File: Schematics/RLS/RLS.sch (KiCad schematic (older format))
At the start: 21 parts, among them J6 ADS1115, U1 ARDUINO_MEGA_SHIELD

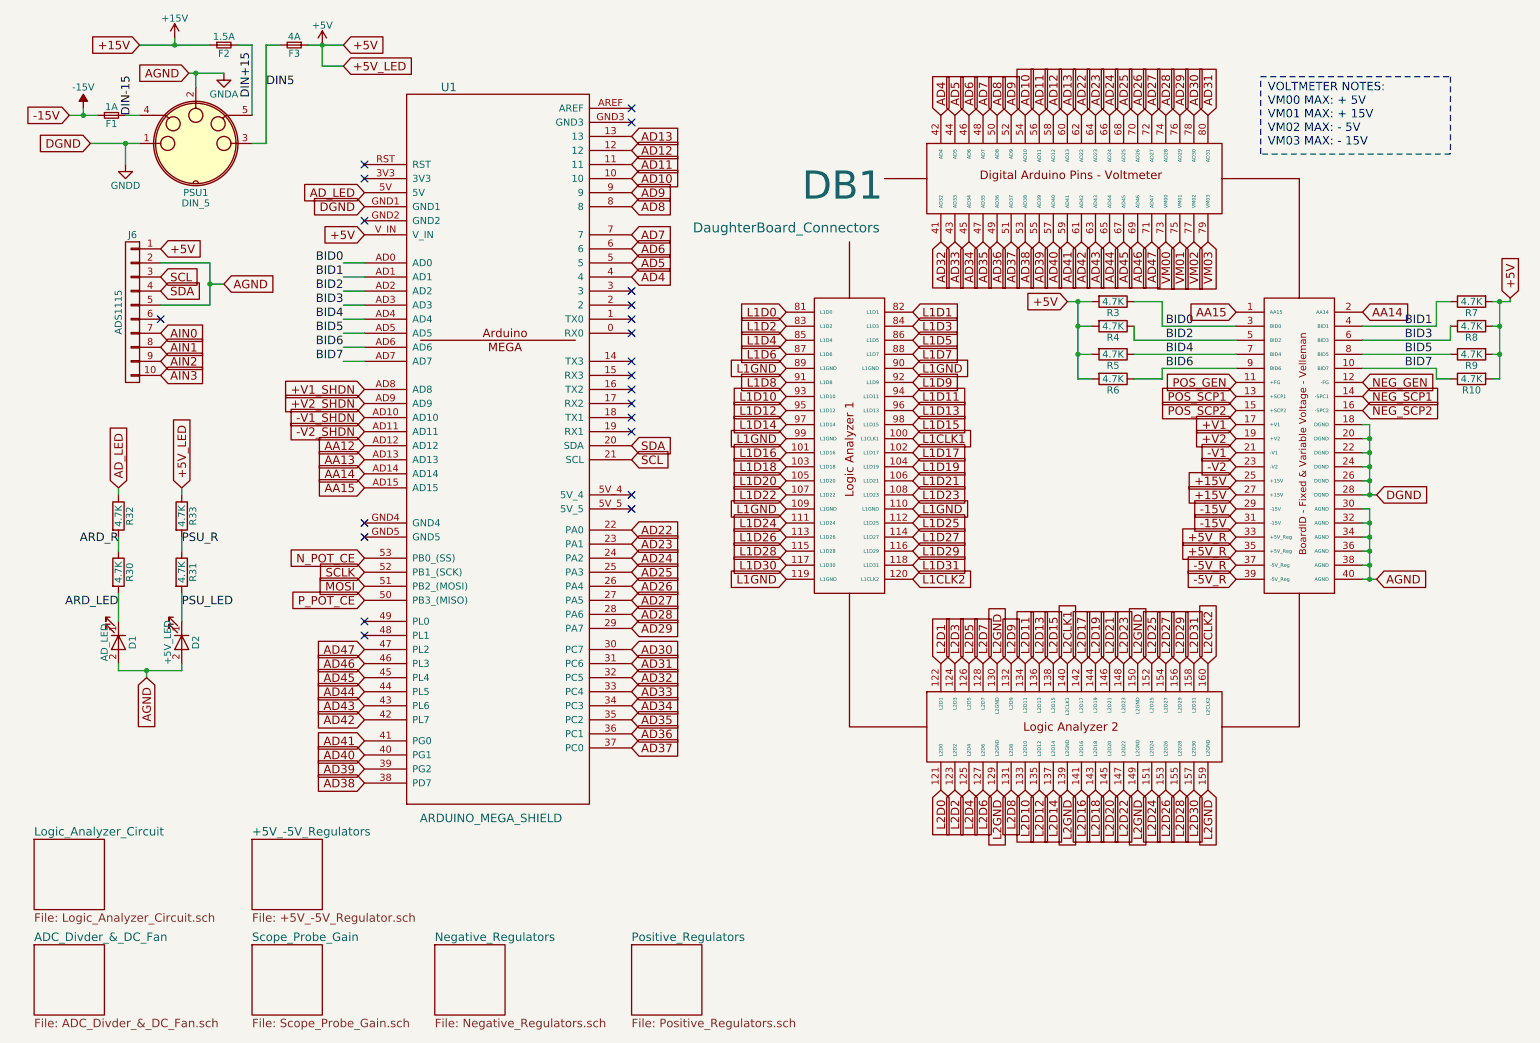
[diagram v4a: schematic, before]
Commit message: Added Things and Fixed Schematic
Added pots to schematic and pcb for adc balancing.
Fixed the component annotation and netlist in the pcb.
Shrunk the pcb down a bit.
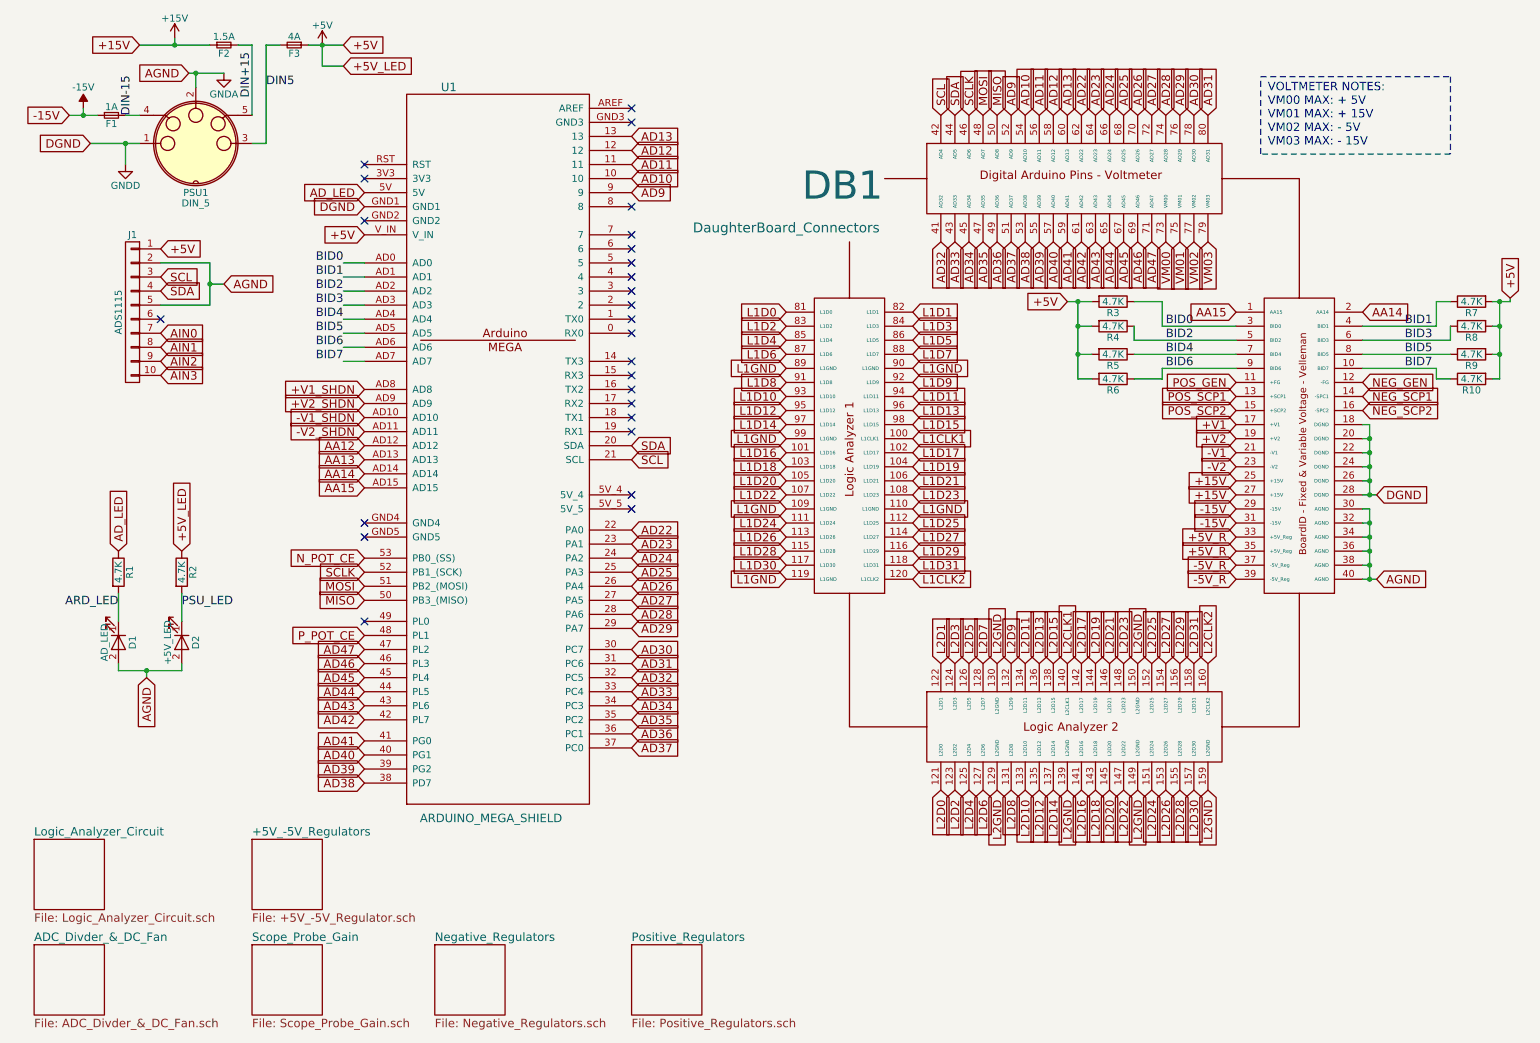
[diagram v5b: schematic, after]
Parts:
- removed R32, R33: 4.7K, Resistors_SMD:R_0805_HandSoldering, symbol R
- renumbered J6 to J1, R30 to R1, R31 to R2
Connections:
- net ARD_R is gone; now on net AD_LED: R1.1
- net PSU_R is gone; now on net +5V: R2.1
- net MOSI: now also DB1.48 (AD7)
- net P_POT_CE: now also U1.48 (PL1); no longer U1.50 (PB3_(MISO))
- net SCL: now also DB1.42 (AD4)
- net SCLK: now also DB1.46 (AD6)
- net SDA: now also DB1.44 (AD5)
- net AD4: no longer names the net of U1.4
- net AD4: no longer DB1.42 (AD4)
- net AD5: no longer names the net of U1.5
- net AD5: no longer DB1.44 (AD5)
- net AD6: no longer names the net of U1.6
- net AD6: no longer DB1.46 (AD6)
- net AD7: no longer names the net of U1.7
- net AD7: no longer DB1.48 (AD7)
- net AD8: no longer names the net of U1.8
- net AD8: no longer DB1.50 (AD8)
- new net MISO: DB1.50 (AD8), U1.50 (PB3_(MISO))
- no-connect marks 22 -> 26
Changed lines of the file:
@@
 $EndDescr
 Text GLabel 7050 1250 1    60   Input ~ 0
-AD4
+SCL
 Text GLabel 7150 1250 1    60   Input ~ 0
-AD5
+SDA
 Text GLabel 7250 1250 1    60   Input ~ 0
-AD6
+SCLK
 Text GLabel 7350 1250 1    60   Input ~ 0
-AD7
+MOSI
 Text GLabel 7450 1250 1    60   Input ~ 0
-AD8
+MISO
 Text GLabel 7550 1250 1    60   Input ~ 0
 AD9
@@
 Text GLabel 7050 6050 3    60   Input ~ 0
 L2D0
-Text GLabel 4850 2400 2    60   Input ~ 0
-AD4
-Text GLabel 4850 2300 2    60   Input ~ 0
-AD5
-Text GLabel 4850 2200 2    60   Input ~ 0
-AD6
-Text GLabel 4850 2100 2    60   Input ~ 0
-AD7
-Text GLabel 4850 1900 2    60   Input ~ 0
-AD8
 Text GLabel 4850 1800 2    60   Input ~ 0
 AD9
@@
 $EndComp
 $Comp
-L CONN_01X10 J6
+L CONN_01X10 J1
 U 1 1 594B108D
 P 1300 2650
-F 0 "J6" H 1300 3200 50  0000 C CNN
+F 0 "J1" H 1300 3200 50  0000 C CNN
 F 1 "ADS1115" V 1400 2650 50  0000 C CNN
 F 2 "Pin_Headers:Pin_Header_Straight_1x10_Pitch2.54mm" H 1300 2650 50  0001 C CNN
@@
 Text GLabel 2950 4400 0    60   Input ~ 0
 N_POT_CE
-Text GLabel 2950 4700 0    60   Input ~ 0
+Text GLabel 2950 4950 0    60   Input ~ 0
 P_POT_CE
 Text GLabel 2950 4500 0    60   Input ~ 0
@@
 NoConn ~ 2950 4250
 NoConn ~ 2950 4850
-NoConn ~ 2950 4950
 NoConn ~ 2950 2000
 NoConn ~ 2950 1700
@@
 $EndComp
 $Comp
-L R R30
+L R R1
 U 1 1 595DC99A
 P 1200 4500
-F 0 "R30" V 1280 4500 50  0000 C CNN
+F 0 "R1" V 1280 4500 50  0000 C CNN
 F 1 "4.7K" V 1200 4500 50  0000 C CNN
 F 2 "Resistors_SMD:R_0805_HandSoldering" V 1130 4500 50  0001 C CNN
@@
 $EndComp
 $Comp
-L R R31
+L R R2
 U 1 1 595DCB07
 P 1650 4500
-F 0 "R31" V 1730 4500 50  0000 C CNN
+F 0 "R2" V 1730 4500 50  0000 C CNN
 F 1 "4.7K" V 1650 4500 50  0000 C CNN
 F 2 "Resistors_SMD:R_0805_HandSoldering" V 1580 4500 50  0001 C CNN
@@
 Text GLabel 2950 1800 0    60   Input ~ 0
 AD_LED
-Text GLabel 1200 3900 1    60   Input ~ 0
+Text GLabel 1200 4350 1    60   Input ~ 0
 AD_LED
-Text GLabel 1650 3900 1    60   Input ~ 0
+Text GLabel 1650 4350 1    60   Input ~ 0
 +5V_LED
 Text GLabel 1400 5250 3    60   Input ~ 0
@@
 	2150 750  2050 750
 Wire Wire Line
-	850  1250 950  1250
-Wire Wire Line
-	950  1250 1050 1250
-Wire Wire Line
-	1350 750  1600 750
-Wire Wire Line
-	1600 750  1850 750
+	850  1250 1050 1250
+Wire Wire Line
+	1350 750  1850 750
 Wire Wire Line
 	1350 1250 1250 1250
@@
 	1500 2300 1850 2300
 Wire Wire Line
-	1850 2300 1850 2450
-Wire Wire Line
-	1850 2450 1850 2600
+	1850 2300 1850 2600
 Wire Wire Line
 	1850 2600 1500 2600
@@
 Connection ~ 1850 2450
 Wire Wire Line
-	10975 2575 11025 2575
-Wire Wire Line
-	11025 2575 11100 2575
-Wire Wire Line
-	11025 2575 11025 2750
-Wire Wire Line
-	11025 2750 11025 2950
-Wire Wire Line
-	11025 2950 11025 3125
+	10975 2575 11100 2575
+Wire Wire Line
+	11025 2575 11025 3125
 Wire Wire Line
 	11025 3125 10975 3125
@@
 	9325 1525 9325 975
 Wire Wire Line
-	1700 950  1750 950
-Wire Wire Line
-	1750 950  1950 950
+	1700 950  1950 950
 Wire Wire Line
 	1750 950  1750 1050
 Wire Wire Line
-	1000 1450 1250 1450
-Wire Wire Line
-	1250 1450 1350 1450
+	1000 1450 1350 1450
 Wire Wire Line
 	1250 1450 1250 1600
@@
 Connection ~ 1750 950
 Wire Wire Line
-	10100 4050 10100 4150
-Wire Wire Line
-	10100 4150 10100 4250
-Wire Wire Line
-	10100 4250 10100 4350
-Wire Wire Line
-	10100 4350 10100 4450
-Wire Wire Line
-	10100 4450 10100 4550
-Wire Wire Line
-	10050 4550 10100 4550
-Wire Wire Line
-	10100 4550 10150 4550
+	10100 4050 10100 4550
+Wire Wire Line
+	10050 4550 10150 4550
 Wire Wire Line
 	10050 4450 10100 4450
@@
 	10050 3450 10100 3450
 Wire Wire Line
-	10100 3450 10100 3550
-Wire Wire Line
-	10100 3550 10100 3650
-Wire Wire Line
-	10100 3650 10100 3750
-Wire Wire Line
-	10100 3750 10100 3850
-Wire Wire Line
-	10100 3850 10100 3950
-Wire Wire Line
-	10050 3950 10100 3950
-Wire Wire Line
-	10100 3950 10150 3950
+	10100 3450 10100 3950
+Wire Wire Line
+	10050 3950 10150 3950
 Wire Wire Line
 	10050 3850 10100 3850
@@
 	2250 750  2250 1450
 Wire Wire Line
-	2550 750  2650 750
-Wire Wire Line
-	2650 750  2800 750
+	2550 750  2800 750
 Connection ~ 2650 750
 Wire Wire Line
 	1650 5200 1650 5150
 Wire Wire Line
-	1200 5200 1400 5200
-Wire Wire Line
-	1400 5200 1650 5200
+	1200 5200 1650 5200
 Wire Wire Line
 	1200 5200 1200 5150
@@
 	1200 4650 1200 4850
 Wire Wire Line
-	1200 4250 1200 4350
-Wire Wire Line
-	1650 4250 1650 4350
-Wire Wire Line
 	2650 750  2650 900
 Wire Wire Line
 	2650 900  2800 900
 Wire Wire Line
-	1200 3900 1200 3950
-Wire Wire Line
-	1650 3900 1650 3950
-Wire Wire Line
 	10050 2750 10575 2750
 Wire Wire Line
@@
 	10575 3125 10675 3125
 Wire Wire Line
-	7950 2575 8025 2575
-Wire Wire Line
-	8025 2575 8125 2575
-Wire Wire Line
-	8025 2575 8025 2750
-Wire Wire Line
-	8025 2750 8025 2950
-Wire Wire Line
-	8025 2950 8025 3125
+	7950 2575 8125 2575
+Wire Wire Line
+	8025 2575 8025 3125
 Wire Wire Line
 	8025 3125 8125 3125
@@
 Text Label 1650 4750 0    60   ~ 0
 PSU_LED
-Text Label 1650 4300 0    60   ~ 0
-PSU_R
-Text Label 1200 4300 2    60   ~ 0
-ARD_R
-$Comp
-L R R32
-U 1 1 595DF587
-P 1200 4100
-F 0 "R32" V 1280 4100 50  0000 C CNN
-F 1 "4.7K" V 1200 4100 50  0000 C CNN
-F 2 "Resistors_SMD:R_0805_HandSoldering" V 1130 4100 50  0001 C CNN
-F 3 "" H 1200 4100 50  0001 C CNN
-	1    1200 4100
-	1    0    0    -1
-$EndComp
-$Comp
-L R R33
-U 1 1 595DF58E
-P 1650 4100
-F 0 "R33" V 1730 4100 50  0000 C CNN
-F 1 "4.7K" V 1650 4100 50  0000 C CNN
-F 2 "Resistors_SMD:R_0805_HandSoldering" V 1580 4100 50  0001 C CNN
-F 3 "" H 1650 4100 50  0001 C CNN
-	1    1650 4100
-	1    0    0    -1
-$EndComp
+Text GLabel 2950 4700 0    60   Input ~ 0
+MISO
+NoConn ~ 4850 1900
+NoConn ~ 4850 2100
+NoConn ~ 4850 2200
+NoConn ~ 4850 2300
+NoConn ~ 4850 2400
 $EndSCHEMATC

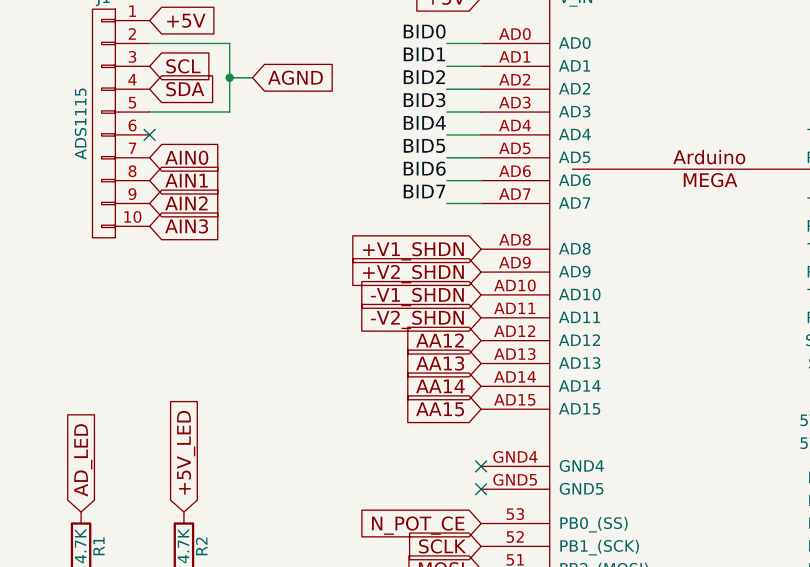
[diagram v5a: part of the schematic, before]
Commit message: MAJOR CHANGE! READ BELOW
Due to layout issues, I changed the pins used for the variable regulator shutdown lines. +V1_SHDN is now AA9, +V2_SHDN is now AA8, -V1_SHDN is now AA11, and -V2_SHDN is now AA10. MAKE SURE TO CHANGE THE RESPECTIVE CODE (Paolo).

Included in this upload is the pre-design review finish PCB and Schematic, with pdf files of each for printing and easy reference.
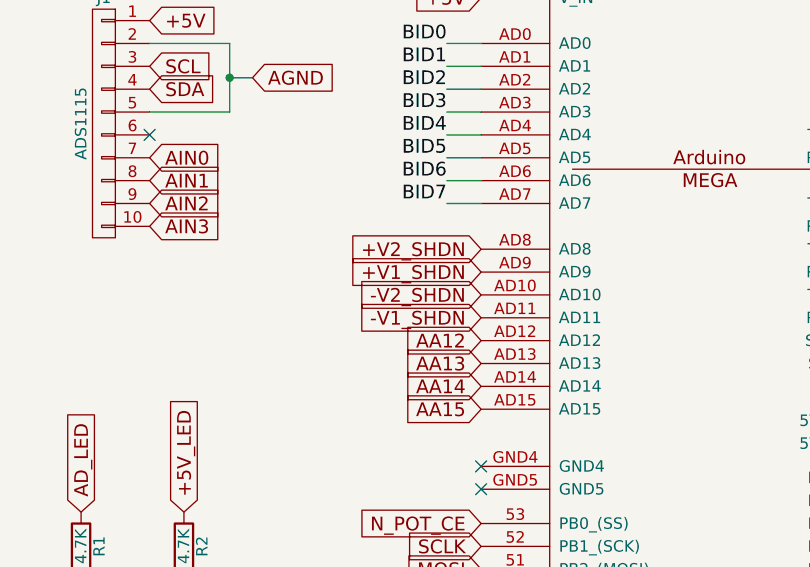
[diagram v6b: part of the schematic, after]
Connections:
- net +V1_SHDN: now also U1.AD9; no longer U1.AD8
- net +V2_SHDN: now also U1.AD8; no longer U1.AD9
- net -V1_SHDN: now also U1.AD11; no longer U1.AD10
- net -V2_SHDN: now also U1.AD10; no longer U1.AD11
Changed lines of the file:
@@
 Sheet 1 7
 Title "Remote Lab System"
-Date ""
-Rev ""
-Comp ""
+Date "2017-07-18"
+Rev "15"
+Comp "University of Washington, Bothell"
 Comment1 ""
 Comment2 ""
@@
 MOSI
 Text GLabel 2950 3200 0    60   Input ~ 0
++V2_SHDN
+Text GLabel 2950 3300 0    60   Input ~ 0
 +V1_SHDN
-Text GLabel 2950 3300 0    60   Input ~ 0
-+V2_SHDN
 Text GLabel 2950 3400 0    60   Input ~ 0
+-V2_SHDN
+Text GLabel 2950 3500 0    60   Input ~ 0
 -V1_SHDN
-Text GLabel 2950 3500 0    60   Input ~ 0
--V2_SHDN
 $Sheet
 S 2150 6400 500  500

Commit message: Finished PCB Need to do Gerbers
It needs to be bought
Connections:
- net AGND: now also D2.1 (K); no longer D1.2 (A), D2.2 (A)
- net ARD_LED: now also D1.2 (A); no longer D1.1 (K)
- net DGND: now also D1.1 (K), U1.GND2
- net PSU_LED: now also D2.2 (A); no longer D2.1 (K)
- no-connect marks 26 -> 25
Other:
- moved on the sheet: D1, D2
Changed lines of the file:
@@
 NoConn ~ 2950 4250
 NoConn ~ 2950 4850
-NoConn ~ 2950 2000
 NoConn ~ 2950 1700
 NoConn ~ 2950 1600
@@
 NoConn ~ 4850 2600
 NoConn ~ 4850 2500
-Text GLabel 2950 1900 0    60   Input ~ 0
+Text GLabel 2900 1900 0    60   Input ~ 0
 DGND
 Text GLabel 2950 2100 0    60   Input ~ 0
@@
 F 3 "" H 1200 5000 50  0001 C CNN
 	1    1200 5000
-	0    1    1    0
+	0    1    -1   0
 $EndComp
 $Comp
@@
 F 3 "" H 1650 5000 50  0001 C CNN
 	1    1650 5000
-	0    1    1    0
+	0    1    -1   0
 $EndComp
 $Comp
@@
 Text GLabel 1650 4350 1    60   Input ~ 0
 +5V_LED
-Text GLabel 1400 5250 3    60   Input ~ 0
+Text GLabel 1650 5200 3    60   Input ~ 0
 AGND
 Text GLabel 2800 900  2    60   Input ~ 0
@@
 	1650 5200 1650 5150
 Wire Wire Line
-	1200 5200 1650 5200
-Wire Wire Line
 	1200 5200 1200 5150
-Wire Wire Line
-	1400 5250 1400 5200
-Connection ~ 1400 5200
 Wire Wire Line
 	1650 4650 1650 4850
@@
 NoConn ~ 4850 2300
 NoConn ~ 4850 2400
+Text GLabel 1200 5200 3    60   Input ~ 0
+DGND
+Wire Wire Line
+	2950 1900 2900 1900
+Wire Wire Line
+	2950 1900 2950 2000
 $EndSCHEMATC
